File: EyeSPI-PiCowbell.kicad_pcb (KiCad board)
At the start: 2 copper layers, 51 x 21 mm, 35 parts, among them J106 EYE_SPI_DISPLAY_FLIP, J107 Conn_01x01, J108 Conn_01x01, J109 Conn_01x01, U101 Pico

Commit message: Production
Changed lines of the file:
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@@
   (paper "A4")
   (title_block
-    (title "EYESPI Feather Wing")
+    (title "EYESPI PiCowbell")
     (date "2023-01-16")
     (rev "1.0.0")
@@
     (fp_line (start 1.6 -1.42) (end -1.6 -1.42) (layer "F.CrtYd") (width 0.05))
     (fp_circle (center 0 0) (end 0.85 0) (layer "F.Fab") (width 0.1) (fill none))
-    (pad "1" thru_hole roundrect (at 0 0) (size 1.85 1.85) (drill 0.85) (layers *.Cu *.Mask) (roundrect_rratio 0.135135)
+    (pad "1" thru_hole roundrect (at 0 0) (size 1.85 1.85) (drill 0.85) (layers *.Cu *.Mask) (roundrect_rratio 0.1351351351)
       (net 11 "/~{MEM_CS}") (pinfunction "Pin_1") (pintype "passive"))
     (model "${KICAD6_3DMODEL_DIR}/Connector_Wire.3dshapes/SolderWire-0.25sqmm_1x01_D0.65mm_OD1.7mm.wrl"
@@
     (fp_line (start 1.6 1.42) (end 1.6 -1.42) (layer "F.CrtYd") (width 0.05))
     (fp_circle (center 0 0) (end 0.85 0) (layer "F.Fab") (width 0.1) (fill none))
-    (pad "1" thru_hole roundrect (at 0 0) (size 1.85 1.85) (drill 0.85) (layers *.Cu *.Mask) (roundrect_rratio 0.135135)
+    (pad "1" thru_hole roundrect (at 0 0) (size 1.85 1.85) (drill 0.85) (layers *.Cu *.Mask) (roundrect_rratio 0.1351351351)
       (net 19 "/EYESPI_GPIO1") (pinfunction "Pin_1") (pintype "passive"))
     (model "${KICAD6_3DMODEL_DIR}/Connector_Wire.3dshapes/SolderWire-0.25sqmm_1x01_D0.65mm_OD1.7mm.wrl"
@@
     (fp_line (start -1.6 -1.42) (end 1.6 -1.42) (layer "B.CrtYd") (width 0.05))
     (fp_circle (center 0 0) (end 0.85 0) (layer "B.Fab") (width 0.1) (fill none))
-    (pad "1" thru_hole roundrect (at 0 0 180) (size 1.85 1.85) (drill 0.85) (layers *.Cu *.Mask) (roundrect_rratio 0.135135)
+    (pad "1" thru_hole roundrect (at 0 0 180) (size 1.85 1.85) (drill 0.85) (layers *.Cu *.Mask) (roundrect_rratio 0.1351351351)
       (net 20 "/EYESPI_GPIO2") (pinfunction "Pin_1") (pintype "passive"))
     (model "${KICAD6_3DMODEL_DIR}/Connector_Wire.3dshapes/SolderWire-0.25sqmm_1x01_D0.65mm_OD1.7mm.wrl"

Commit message: Closes #1 #2 #3
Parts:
- added J101: StemmaQT, Connector_JST:JST_SH_SM04B-SRSS-TB_1x04-1MP_P1.00mm_Horizontal, F.Cu at (180.0, 72.2)
- added SW101: SW_Push, Footprints:Switch_SMD_3.95x2.9mm, F.Cu at (180.0, 64.7)
- J106: value EYE_SPI_DISPLAY_FLIP -> EYE_SPI_DISPLAY_TYPE_B
- moved R101 41.8 mm to (180.0, 78.5)
- moved D101 39.0 mm to (180.0, 80.3), turned to 0 degrees
- moved kibuzzard-63C5DDB7 9.87 mm to (144.1, 72.7), turned to 90 degrees
- moved J109 8.26 mm to (144.2, 77.0)
- moved J108 2.12 mm to (150.7, 77.0)
- moved J107 2.12 mm to (147.5, 77.0)
- moved kibuzzard-63C5DDAE 2.11 mm to (150.7, 73.9)
- moved kibuzzard-63C5DD9E 2.09 mm to (147.4, 73.9)
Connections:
- J106 pad 1: +3V3 -> /EYESPI_GPIO2
- J106 pad 10: /~{CARD_CS} -> /~{TFT_CS}
- J106 pad 11: /~{MEM_CS} -> /~{TFT_RST}
- J106 pad 12: /~{TS_CS} -> /TFT_DC
- J106 pad 13: /EYESPI_SCL -> /EYESPI_MISO
- J106 pad 14: /EYESPI_SDA -> /EYESPI_MOSI
- J106 pad 15: /INT -> /EYESPI_SCK
- J106 pad 16: /BUSY -> GND
- J106 pad 17: /EYESPI_GPIO1 -> /LITE
- J106 pad 18: /EYESPI_GPIO2 -> +3V3
- J106 pad 2: /LITE -> /EYESPI_GPIO1
- J106 pad 3: GND -> /BUSY
- J106 pad 4: /EYESPI_SCK -> /INT
- J106 pad 5: /EYESPI_MOSI -> /EYESPI_SDA
- J106 pad 6: /EYESPI_MISO -> /EYESPI_SCL
- J106 pad 7: /TFT_DC -> /~{TS_CS}
- J106 pad 8: /~{TFT_RST} -> /~{MEM_CS}
- J106 pad 9: /~{TFT_CS} -> /~{CARD_CS}
- U101 pad 30: unconnected-(U101-Pad30) -> /~{RUN}
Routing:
- net +3V3: track 9.73 -> 124.9 mm
- net SDA: track 2.32 -> 50.0 mm, vias 0 -> 1
- net GND: track 107.1 -> 152.5 mm, vias 1 -> 11
- net SCL: track 2.31 -> 46.5 mm, vias 0 -> 1
- net /~{RUN}: track 0.00 -> 28.4 mm
- net /~{MEM_CS}: track 31.5 -> 16.3 mm
- net /LITE: track 3.33 -> 14.9 mm
- net /~{TS_CS}: track 34.6 -> 45.5 mm, vias 0 -> 2
- net unconnected-(J101-PadMP): track 0.00 -> 5.60 mm
- net /EYESPI_SCL: track 9.25 -> 14.8 mm, vias 0 -> 2
- net /EYESPI_SDA: track 6.64 -> 11.8 mm, vias 0 -> 2
- net /EYESPI_GPIO1: track 17.6 -> 21.5 mm
- net /~{TFT_CS}: track 42.5 -> 39.7 mm
- net /~{TFT_RST}: track 30.0 -> 27.2 mm, vias 2 -> 0
- net /~{CARD_CS}: track 21.9 -> 23.5 mm
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- added copper zone on F.Cu, net GND
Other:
- board size 51 x 21 mm -> 59.3 x 21 mm

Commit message: Production
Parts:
- added kibuzzard-63E91FEA: G***, kibuzzard-63E91FEA, F.Cu at (125.5, 72.1)
- R101: value 1K -> 330R

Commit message: Closed #4 update to KiCad 7
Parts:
- removed kibuzzard-63C5DCBF: G***, kibuzzard-63C5DCBF
- removed kibuzzard-63C5DCD9: G***, kibuzzard-63C5DCD9
- removed kibuzzard-63C5DCE3: G***, kibuzzard-63C5DCE3
- removed kibuzzard-63C5DCEE: G***, kibuzzard-63C5DCEE
- removed kibuzzard-63C5DCF9: G***, kibuzzard-63C5DCF9
- removed kibuzzard-63C5DD0E: G***, kibuzzard-63C5DD0E
- removed kibuzzard-63C5DD7B: G***, kibuzzard-63C5DD7B
- removed kibuzzard-63C5DD88: G***, kibuzzard-63C5DD88
- removed kibuzzard-63C5DD93: G***, kibuzzard-63C5DD93
- removed kibuzzard-63C5DD9E: G***, kibuzzard-63C5DD9E
- removed kibuzzard-63C5DDAE: G***, kibuzzard-63C5DDAE
- removed kibuzzard-63C5DDB7: G***, kibuzzard-63C5DDB7
- removed kibuzzard-63C5F2BE: G***, kibuzzard-63C5F2BE
- removed kibuzzard-63C5F2D1: G***, kibuzzard-63C5F2D1
- removed kibuzzard-63C5F2E8: G***, kibuzzard-63C5F2E8
- removed kibuzzard-63E91FEA: G***, kibuzzard-63E91FEA
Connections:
- J101 pad 3: SCL -> SDA
- J101 pad 4: SDA -> SCL
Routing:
- net GND: track 152.5 -> 154.7 mm
- net SCL: track 46.5 -> 48.5 mm
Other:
- board text added: "BUSY"
- board text added: "CARD_CS"
- board text added: "INT"
- board text added: "IO1"
- board text added: "IO2"
- board text added: "MEM_CS"
- board text added: "MISO"
- board text added: "MOSI"
- board text added: "SCK"
- board text added: "SCL"
- board text added: "SDA"
- board text added: "TFT_CS"
- board text added: "TFT_DC"
- board text added: "TFT_RST"
- board text added: "TS_CS"
- board text added: "Type B Connector"

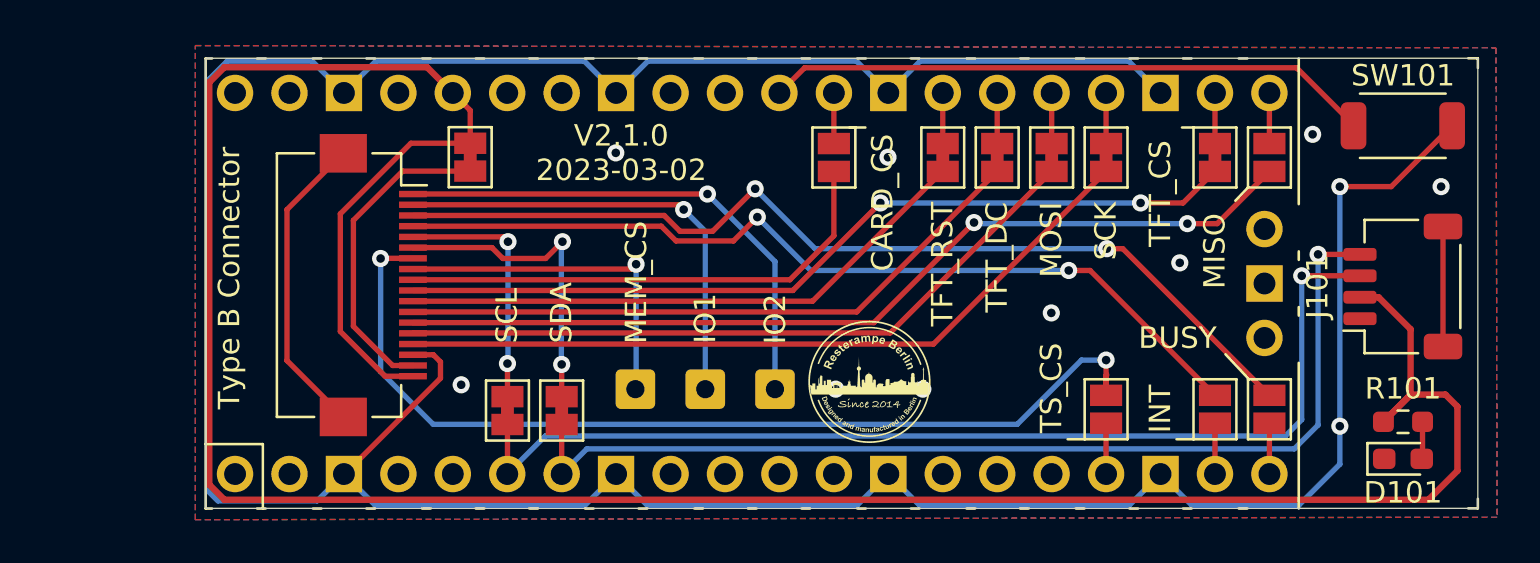
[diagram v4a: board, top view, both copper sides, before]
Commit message: Placed FPC connector outside Pico
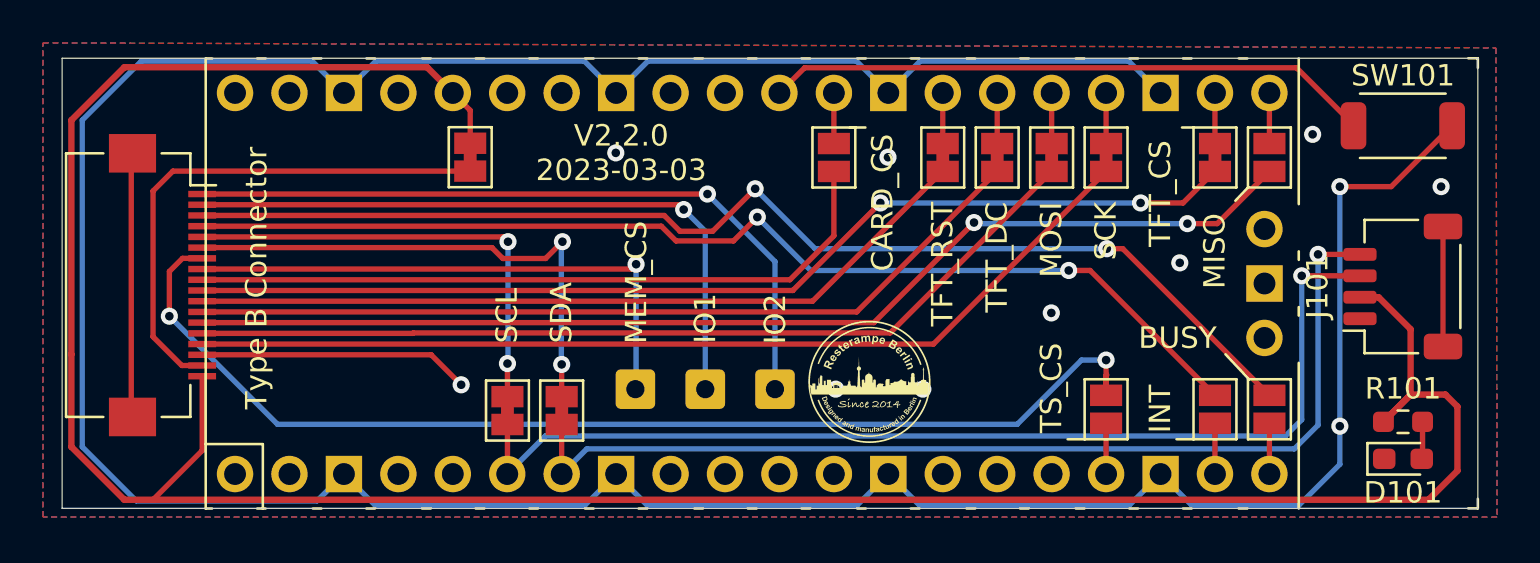
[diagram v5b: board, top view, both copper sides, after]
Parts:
- moved J106 9.84 mm to (122.1, 72.2)
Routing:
- net GND: track 154.7 -> 168.3 mm
- net /LITE: track 14.9 -> 24.8 mm
- net /EYESPI_SCL: track 14.8 -> 24.6 mm
- net /EYESPI_GPIO1: track 21.5 -> 31.4 mm
- net /~{TFT_RST}: track 27.2 -> 37.1 mm
- net /~{TFT_CS}: track 39.7 -> 49.6 mm
- net /~{MEM_CS}: track 16.3 -> 26.2 mm
- net /~{CARD_CS}: track 23.5 -> 33.3 mm
- net /INT: track 41.6 -> 51.4 mm
- net /EYESPI_SCK: track 35.7 -> 45.5 mm
- net /EYESPI_MOSI: track 32.9 -> 42.8 mm
- net /EYESPI_MISO: track 42.9 -> 52.8 mm
- net /BUSY: track 45.1 -> 54.9 mm
- net /EYESPI_SDA: track 11.8 -> 21.6 mm
- net /TFT_DC: track 30.0 -> 39.8 mm
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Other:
- board size 59.3 x 21 mm -> 66.1 x 21 mm
